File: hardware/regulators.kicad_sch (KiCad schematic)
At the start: 16 parts, among them U10 AMS1117-3.3, U9 LM5163DDA

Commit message: Power Layout
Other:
- title: (none) -> GreenMobi Drive
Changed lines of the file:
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@@
 	(generator_version "9.0")
 	(paper "A4")
+	(title_block
+		(title "GreenMobi Drive")
+		(date "2025-07-02")
+		(rev "0.1")
+	)
 	(rectangle
 		(start 80.01 113.03)

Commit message: Added IMU
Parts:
- C30: footprint (none) -> Capacitor_SMD:C_0402_1005Metric
- C31: value C -> 56p; footprint (none) -> Capacitor_SMD:C_0603_1608Metric
- C32: value C -> 3.3n; footprint (none) -> Capacitor_SMD:C_0603_1608Metric
- L2: value L -> 6.8u
- R45, R46: value R -> 453k; footprint Resistor_SMD:R_0402_1005Metric -> Resistor_SMD:R_0603_1608Metric
- R47: value R -> 49.9
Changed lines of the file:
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@@
 			)
 		)
-		(property "Value" "C"
+		(property "Value" "3.3n"
 			(at 162.56 80.01 90)
 			(effects
@@
 			)
 		)
-		(property "Footprint" ""
+		(property "Footprint" "Capacitor_SMD:C_0603_1608Metric"
 			(at 162.56 82.55 0)
 			(effects
@@
 			)
 		)
-		(property "Value" "L"
+		(property "Value" "6.8u"
 			(at 158.75 72.39 90)
 			(effects
@@
 		(fields_autoplaced yes)
 		(property "Reference" "C30"
-			(at 147.32 71.1263 0)
+			(at 147.32 71.1262 0)
 			(effects
 				(font
@@
 		)
 		(property "Value" "2.2n"
-			(at 147.32 73.6663 0)
+			(at 147.32 73.6662 0)
 			(effects
 				(font
@@
 			)
 		)
-		(property "Footprint" ""
+		(property "Footprint" "Capacitor_SMD:C_0402_1005Metric"
 			(at 144.78 72.39 0)
 			(effects
@@
 			)
 		)
-		(property "Value" "R"
+		(property "Value" "49.9"
 			(at 177.8 96.5199 0)
 			(effects
@@
 			)
 		)
-		(property "Value" "R"
+		(property "Value" "453k"
 			(at 177.8 83.8199 0)
 			(effects
@@
 			)
 		)
-		(property "Footprint" "Resistor_SMD:R_0402_1005Metric"
+		(property "Footprint" "Resistor_SMD:R_0603_1608Metric"
 			(at 175.26 82.55 0)
 			(effects
@@
 			)
 		)
-		(property "Value" "C"
+		(property "Value" "56p"
 			(at 161.29 88.9062 0)
 			(effects
@@
 			)
 		)
-		(property "Footprint" ""
+		(property "Footprint" "Capacitor_SMD:C_0603_1608Metric"
 			(at 158.75 87.63 0)
 			(effects
@@
 			)
 		)
-		(property "Value" "R"
+		(property "Value" "453k"
 			(at 154.94 80.01 90)
 			(effects
@@
 			)
 		)
-		(property "Footprint" "Resistor_SMD:R_0402_1005Metric"
+		(property "Footprint" "Resistor_SMD:R_0603_1608Metric"
 			(at 154.94 82.55 0)
 			(effects

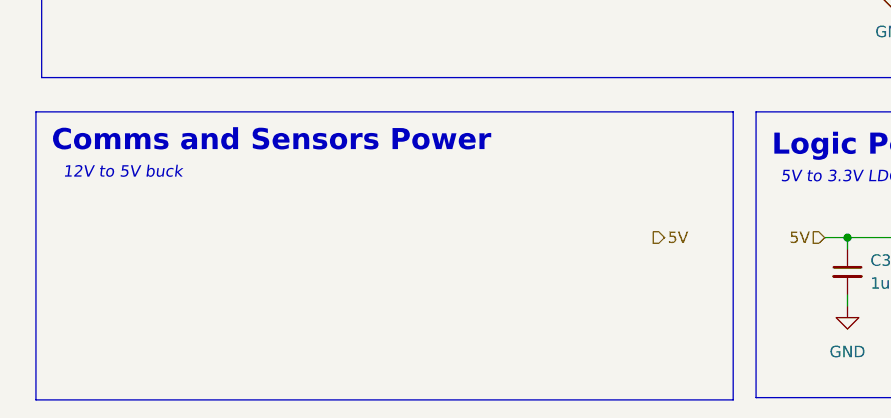
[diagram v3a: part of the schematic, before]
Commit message: 5V regulator
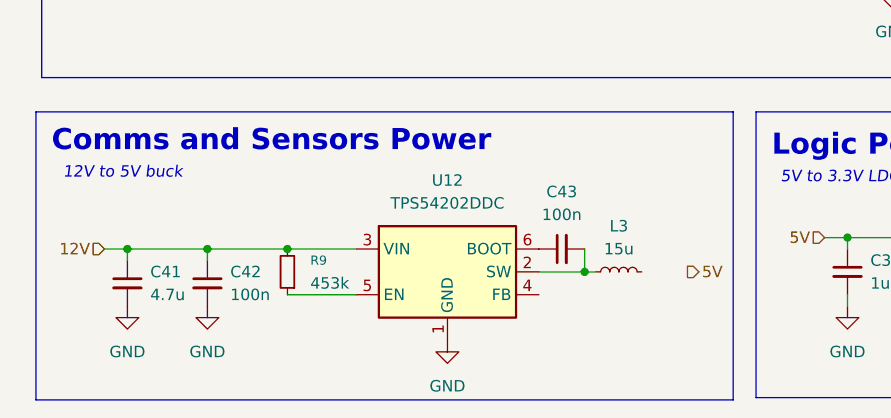
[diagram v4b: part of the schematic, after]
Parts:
- added C41: 4.7u, Capacitor_SMD:C_0805_2012Metric, symbol Device:C_Small
- added C42: 100n, Capacitor_SMD:C_0402_1005Metric, symbol Device:C_Small
- added C43: 100n, symbol Device:C_Small
- added L3: 15u, symbol Device:L_Small
- added R9: 453k, symbol Device:R_Small
- added U12: TPS54202DDC, Package_TO_SOT_SMD:SOT-23-6, symbol Regulator_Switching:TPS54202DDC
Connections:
- net 12V: now also C41.1, C42.1, R9.2, U12.3 (VIN)
- net GND: now also C41.2, C42.2, U12.1 (GND)
- new net: C43.2, L3.1, U12.2 (SW)
- new net: R9.1, U12.5 (EN)
- new net: C43.1, U12.6 (BOOT)

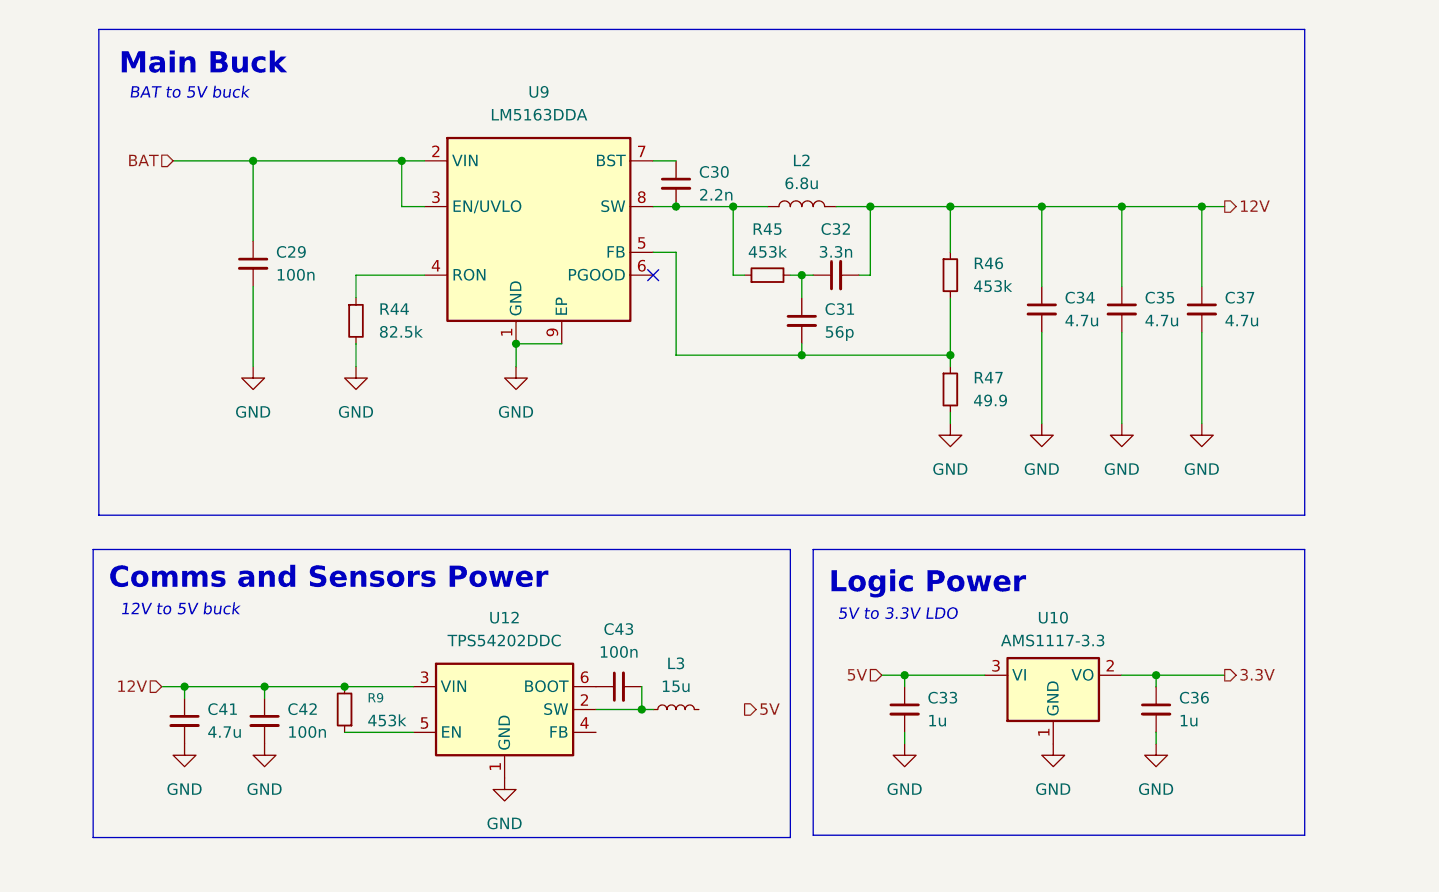
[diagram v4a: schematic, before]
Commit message: Regulators layout
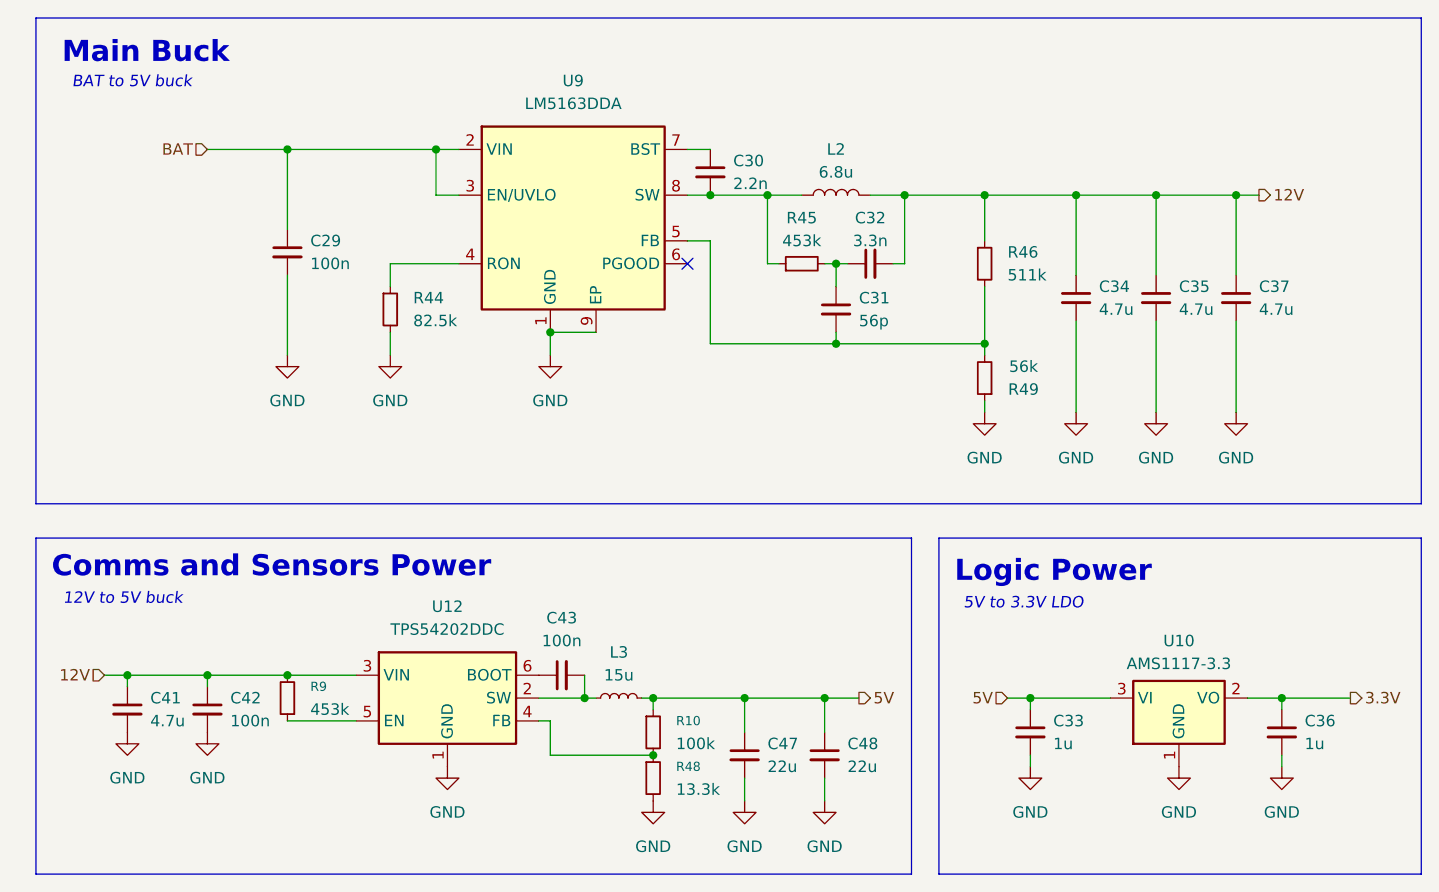
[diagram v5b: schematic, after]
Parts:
- removed R47: 49.9, Resistor_SMD:R_0402_1005Metric, symbol Device:R_Small
- added C47, C48: 22u, Capacitor_SMD:C_0805_2012Metric, symbol Device:C_Small
- added R10: 100k, Resistor_SMD:R_0402_1005Metric, symbol Device:R_Small
- added R48: 13.3k, Resistor_SMD:R_0402_1005Metric, symbol Device:R_Small
- added R49: 56k, Resistor_SMD:R_0805_2012Metric, symbol Device:R_Small
- C33, C36: footprint Capacitor_SMD:C_0402_1005Metric -> Capacitor_SMD:C_1206_3216Metric
- C43: footprint (none) -> Capacitor_SMD:C_0402_1005Metric
- L3: footprint (none) -> Inductor_SMD:L_Chilisin_BMRA00040420
- R46: value 453k -> 511k
- R9: footprint (none) -> Resistor_SMD:R_0402_1005Metric
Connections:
- net 5V: now also L3.2, C47.1, C48.1, R10.1
- net GND: now also C47.2, C48.2, R48.2, R49.1
- net at U12.4 (FB): now also R10.2, R48.1
- net at C31.2, R46.2, U9.5 (FB): now also R49.2
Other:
- moved on the sheet: C29, C30, C31, C32, C33, C34, C35, C36, C37, C41, C42, C43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

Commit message: BOM optimizations
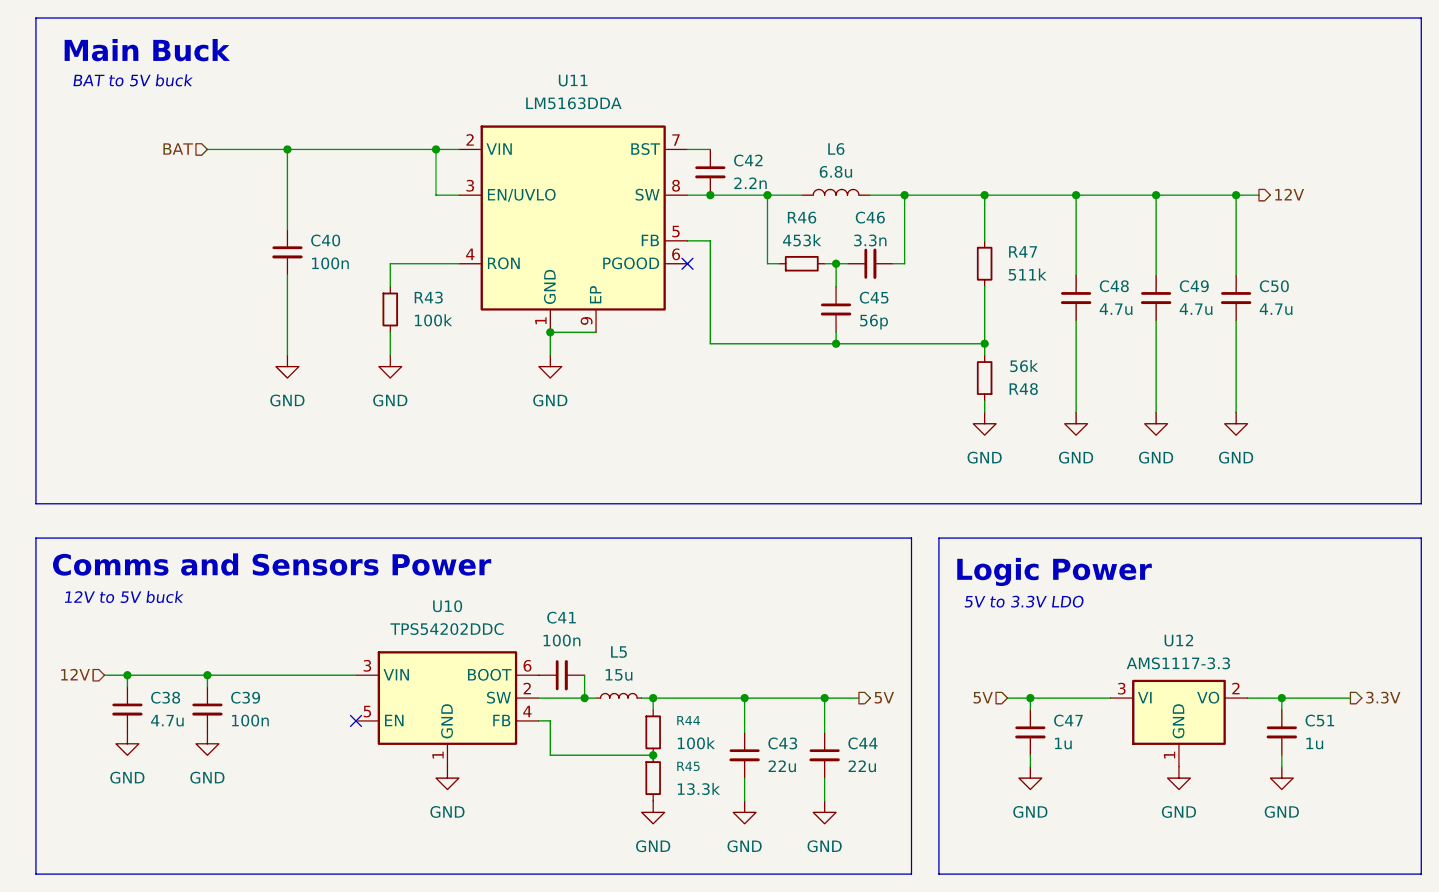
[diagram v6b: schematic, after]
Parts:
- removed R9: 453k, Resistor_SMD:R_0402_1005Metric, symbol Device:R_Small
- R43: renamed from R44; value 82.5k -> 100k
- renumbered C41 to C38, C42 to C39, C29 to C40, C43 to C41, C30 to C42, C47 to C43, C48 to C44, C31 to C45, C32 to C46, C33 to C47, C34 to C48, C35 to C49, C37 to C50, C36 to C51, L3 to L5, L2 to L6, R10 to R44, R48 to R45, R45 to R46, R46 to R47, R49 to R48, U12 to U10, U9 to U11, U10 to U12
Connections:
- no-connect marks 1 -> 2

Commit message: Capacitors sourced
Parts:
- C38, C48, C49, C50: LCSC (none) -> C1779
- C39, C41: LCSC (none) -> C77020
- C40: LCSC (none) -> C110255
- C42: LCSC (none) -> C106861
- C43, C44: LCSC (none) -> C476766
- C45: LCSC (none) -> C1676
- C46: LCSC (none) -> C107088
- C47, C51: LCSC (none) -> C28322
- U12: LCSC (none) -> C6186

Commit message: Sourcing complete
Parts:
- L5: LCSC (none) -> C2894719
- R43, R44: LCSC (none) -> C60491
- R46: LCSC (none) -> C3013202
- R47: LCSC (none) -> C2930114
- R48: LCSC (none) -> C17756
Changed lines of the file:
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@@
+			)
+		)
+		(property "LCSC" "C2894719"
+			(at 138.43 129.54 90)
+			(effects
+				(font
+					(size 1.27 1.27)
+				)
+				(hide yes)
 			)
 		)
@@
 			)
 		)
+		(property "LCSC" "C2930114"
+			(at 179.07 81.28 0)
+			(effects
+				(font
+					(size 1.27 1.27)
+				)
+				(hide yes)
+			)
+		)
 		(pin "1"
 		)
@@
 			)
 		)
+		(property "LCSC" "C60491"
+			(at 142.24 133.35 0)
+			(effects
+				(font
+					(size 1.27 1.27)
+				)
+				(hide yes)
+			)
+		)
 		(pin "2"
 		)
@@
 			)
 		)
+		(property "LCSC" "C60491"
+			(at 113.03 86.36 0)
+			(effects
+				(font
+					(size 1.27 1.27)
+				)
+				(hide yes)
+			)
+		)
 		(pin "1"
 		)
@@
 			)
 		)
+		(property "LCSC" "C3013202"
+			(at 158.75 81.28 90)
+			(effects
+				(font
+					(size 1.27 1.27)
+				)
+				(hide yes)
+			)
+		)
 		(pin "1"
 		)
@@
 			(at 179.07 93.98 0)
 			(effects
+				(font
+					(size 1.27 1.27)
+				)
+				(hide yes)
+			)
+		)
+		(property "LCSC" "C17756"
+			(at 179.07 93.98 0)
+			(effects
